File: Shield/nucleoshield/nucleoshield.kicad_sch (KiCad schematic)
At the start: 21 parts, among them J1 Conn_02x19_Odd_Even, J2 Conn_02x19_Odd_Even

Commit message: Nucleo shield
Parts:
- added J? (x2): Screw_Terminal_01x02, Connector_TE-Connectivity:TE_826576-2_1x02_P3.96mm_Vertical, symbol Connector:Screw_Terminal_01x02
- added JP?: Jumper_3_Open, symbol Jumper:Jumper_3_Open
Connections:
- net Nucleo_3V3 is gone; now on net NUCLEO_3V3: JP?.1 (A)
- net DCDC_3V3: now also J?.1 (Pin_1)
- net 3V3 renamed NUCLEO_3V3
- net 5V renamed NUCLEO_5V
- net NUCLEO_5V: now also JP?.1 (A)
- new net DCDC_5V: J?.1 (Pin_1), JP?.3 (B)
- new net DCDC_GND: J?.2 (Pin_2), J?.2 (Pin_2)
- new net LOGIC_5V: JP?.2 (C)
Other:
- moved on the sheet: C?, D?, IC?, R?

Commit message: Schematic and pcb ready
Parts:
- removed C?: 100n, symbol Device:C
- removed C? (x3): 0.1u, symbol Device:C
- removed IC?: L80-M39, L80-M39, symbol L80-M39:L80-M39
- removed J? (x3): Conn_01x05, Connector_PinSocket_2.54mm:PinSocket_1x05_P2.54mm_Vertical, symbol Connector_Generic:Conn_01x05
- removed J? (x2): Screw_Terminal_01x02, Connector_TE-Connectivity:TE_826576-2_1x02_P3.96mm_Vertical, symbol Connector:Screw_Terminal_01x02
- removed JP? (x2): Jumper_3_Open, symbol Jumper:Jumper_3_Open
- removed R? (x2): R, symbol Device:R
- removed U?: ICM-20948, Sensor_Motion:InvenSense_QFN-24_3x3mm_P0.4mm, symbol Sensor_Motion:ICM-20948
- added C1, C5: 470u, Capacitor_THT:CP_Radial_D8.0mm_P3.50mm, symbol Device:C_Polarized
- added C2: 47u, Capacitor_SMD:C_1206_3216Metric, symbol Device:C
- added C3, C4: 100n, Capacitor_SMD:C_1206_3216Metric, symbol Device:C
- added IC1: L80-M39, componentLib:L80-M39, symbol L80-M39:L80-M39
- added J11: MPU9250, Connector_PinHeader_2.54mm:PinHeader_1x10_P2.54mm_Vertical, symbol Connector_Generic:Conn_01x10
- added J3: POWER, Connector_PinHeader_2.54mm:PinHeader_1x03_P2.54mm_Vertical, symbol Connector_Generic:Conn_01x03
- added J4: MOTOR_1, Connector_PinSocket_2.54mm:PinSocket_1x04_P2.54mm_Vertical, symbol Connector_Generic:Conn_01x04
- added J7: MOTOR_2, Connector_PinSocket_2.54mm:PinSocket_1x04_P2.54mm_Vertical, symbol Connector_Generic:Conn_01x04
- added J8: LCD_I2C, Connector_PinSocket_2.54mm:PinSocket_1x04_P2.54mm_Vertical, symbol Connector_Generic:Conn_01x04
- added J9: MOTOR_3, Connector_PinSocket_2.54mm:PinSocket_1x04_P2.54mm_Vertical, symbol Connector_Generic:Conn_01x04
- added JP1: AVDD-3.3V, Jumper:SolderJumper-2_P1.3mm_Bridged2Bar_Pad1.0x1.5mm, symbol Jumper:Jumper_2_Bridged
- added Q1, Q2: BSS138, Package_TO_SOT_SMD:SOT-23, symbol Transistor_FET:BSS138
- added R1: 10k, Resistor_SMD:R_0805_2012Metric, symbol Device:R
- added R2: 2k, Resistor_SMD:R_0805_2012Metric, symbol Device:R
- added R3, R4, R5, R6: 2K, Resistor_SMD:R_0805_2012Metric, symbol Device:R
- added TP1: AVDD, TestPoint:TestPoint_THTPad_1.0x1.0mm_Drill0.5mm, symbol Connector:TestPoint
- C6, C7: renamed from C?; footprint (none) -> Capacitor_SMD:C_1206_3216Metric
- D1: renamed from D?; footprint (none) -> LED_SMD:LED_0805_2012Metric
- J10: renamed from J?; value Conn_01x04 -> ENCODER_3; footprint (none) -> Connector_PinSocket_2.54mm:PinSocket_1x04_P2.54mm_Vertical
- J5: renamed from J?; value Conn_01x04 -> ENCODER_1
- J6: renamed from J?; value Conn_01x04 -> ENCODER_2; footprint (none) -> Connector_PinSocket_2.54mm:PinSocket_1x04_P2.54mm_Vertical
- R7: renamed from R?; value R -> 1K; footprint (none) -> Resistor_SMD:R_0805_2012Metric
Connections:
- net GND is gone; now on net ENCODER_GND: J1.19 (Pin_19), J1.20 (Pin_20), J1.22 (Pin_22), J1.8 (Pin_8), J2.20 (Pin_20), J2.9 (Pin_9)
- net LOGIC_GND is gone; now on net ENCODER_GND: C6.1, C7.1, D1.1 (K)
- net NUCLEO_3V3 is gone; now on net ENCODER_VCC: J1.16 (Pin_16)
- net NUCLEO_5V is gone; now on net LOGIC_5V: J1.18 (Pin_18)
- net AVDD: now also JP1.1 (A), TP1.1
- net E5V: now also J3.2 (5V_DCDC)
- net ENCODER_A1: now also J1.23 (Pin_23), J5.3 (Pin_3); no longer J5.2 (Pin_2)
- net ENCODER_A2: now also J1.27 (Pin_27), J6.3 (Pin_3); no longer J6.2 (Pin_2)
- net ENCODER_A3: now also J1.31 (Pin_31), J10.3 (Pin_3); no longer J10.2 (Pin_2)
- net ENCODER_B1: now also J1.25 (Pin_25), J5.4 (Pin_4); no longer J5.1 (Pin_1)
- net ENCODER_B2: now also J1.29 (Pin_29), J6.4 (Pin_4); no longer J6.1 (Pin_1)
- net ENCODER_B3: now also J1.35 (Pin_35), J10.4 (Pin_4); no longer J10.1 (Pin_1)
- net ENCODER_GND: now also J10.2 (Pin_2), J5.2 (Pin_2), J6.2 (Pin_2), C1.2, C2.1, C3.2, C4.2, C5.2, IC1.12 (GND_2), IC1.3 (GND_1), J11.2 (Pin_2), J3.3 (GND), J4.2 (Pin_2), J7.2 (Pin_2), J8.2 (Pin_2), J9.2 (Pin_2), R2.2; no longer J10.3 (Pin_3), J10.4 (Pin_4), J5.3 (Pin_3), J5.4 (Pin_4), J6.3 (Pin_3), J6.4 (Pin_4)
- net GPS_RESET: now also IC1.10 (RESET)
- net GPS_UART_RX: now also IC1.1 (RXD1)
- net GPS_UART_TX: now also IC1.2 (TXD1)
- net INA1: now also J4.3 (Pin_3)
- net INA2: now also J7.3 (Pin_3)
- net INA3: now also J9.3 (Pin_3)
- net INB1: now also J4.4 (Pin_4)
- net INB2: now also J7.4 (Pin_4)
- net INB3: now also J9.4 (Pin_4)
- net LOGIC_5V: now also C3.1, C5.1, J8.1 (Pin_1), R5.1, R6.1
- net SCL: now also J11.3 (Pin_3)
- net SDA: now also J11.4 (Pin_4)
- net VIN: now also J3.1 (7.2V), R1.1
- net at R7.2: now also IC1.6 (1PPS)
- net BAT_ADC: now reaches J1.38 (Pin_38)
- net BAT_ADC: now also C2.2, R1.2, R2.1
- net SCL2: now reaches J2.25 (Pin_25)
- net SCL2: now also Q2.2 (S), R4.2
- net SDA2: now reaches J2.31 (Pin_31)
- net SDA2: now also Q1.2 (S), R3.2
- net AD0: no longer names the net of J2.15 (Pin_15)
- net AGND: no longer names the net of J2.32 (Pin_32)
- net LOGIC_3V3 renamed ENCODER_VCC
- net ENCODER_VCC: now also J10.1 (Pin_1), J5.1 (Pin_1), J6.1 (Pin_1), C1.1, C4.1, IC1.4 (VCC), IC1.5 (V_BCKP), J11.1 (Pin_1), J4.1 (Pin_1), J7.1 (Pin_1), J9.1 (Pin_1), JP1.2 (B), Q1.1 (G), Q2.1 (G), R3.1, R4.1
- net MODE1: no longer names the net of J2.12 (Pin_12)
- net MODE2: no longer names the net of J2.14 (Pin_14)
- net MODE3: no longer names the net of J2.16 (Pin_16)
- new net: J8.3 (Pin_3), Q1.3 (D), R5.2
- new net: J8.4 (Pin_4), Q2.3 (D), R6.2
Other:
- note added: "5V I2C interface"
- note added: "LCD"
- moved on the sheet: R7

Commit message: power modifications
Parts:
- added JP2: Jumper_3_Open, Connector_PinSocket_2.54mm:PinSocket_1x03_P2.54mm_Vertical, symbol Jumper:Jumper_3_Open
- J10, J4, J5, J6, J7, J8, J9: footprint Connector_PinSocket_2.54mm:PinSocket_1x04_P2.54mm_Vertical -> Connector_JST:JST_EH_B4B-EH-A_1x04_P2.50mm_Vertical
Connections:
- net LOGIC_5V: now also JP2.2 (C); no longer J1.18 (Pin_18)
- net E5V renamed 5V_DCDC
- net 5V_DCDC: now also JP2.3 (B)
- new net NUCLEO_5V: J1.18 (Pin_18), JP2.1 (A)
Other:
- moved on the sheet: C2, C3, C5, J3, JP1, R1, R2, TP1

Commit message: Power connector
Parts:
- added J12, J13: Screw_Terminal_01x02, TerminalBlock:TerminalBlock_Altech_AK300-2_P5.00mm, symbol Connector:Screw_Terminal_01x02
- added JP3: Jumper_3_Open, Connector_PinSocket_2.54mm:PinSocket_1x03_P2.54mm_Vertical, symbol Jumper:Jumper_3_Open
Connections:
- net 5V_DCDC: now also J12.2 (Pin_2)
- net ENCODER_GND: now also J12.1 (Pin_1), J13.1 (Pin_1)
- net ENCODER_VCC: now also JP3.2 (C); no longer J1.16 (Pin_16), JP1.2 (B)
- new net 3V3_DCDC: J13.2 (Pin_2), JP3.3 (B)
- new net NUCLEO_3V3: J1.16 (Pin_16), JP1.2 (B), JP3.1 (A)
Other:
- moved on the sheet: C1, C2, C3, C4, C5, J3, JP1, JP2, R1, R2, TP1

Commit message: small changes
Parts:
- JP2, JP3: footprint Connector_PinSocket_2.54mm:PinSocket_1x03_P2.54mm_Vertical -> Connector_PinHeader_2.54mm:PinHeader_1x03_P2.54mm_Vertical
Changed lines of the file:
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@@
     (property "Reference" "JP2" (id 0) (at 38.1 67.945 0))
     (property "Value" "Jumper_3_Open" (id 1) (at 38.1 70.485 0))
-    (property "Footprint" "Connector_PinSocket_2.54mm:PinSocket_1x03_P2.54mm_Vertical" (id 2) (at 38.1 74.93 0)
+    (property "Footprint" "Connector_PinHeader_2.54mm:PinHeader_1x03_P2.54mm_Vertical" (id 2) (at 38.1 74.93 0)
       (effects (font (size 1.27 1.27)) hide)
     )
@@
     (property "Reference" "JP3" (id 0) (at 33.02 23.495 0))
     (property "Value" "Jumper_3_Open" (id 1) (at 33.02 26.035 0))
-    (property "Footprint" "Connector_PinSocket_2.54mm:PinSocket_1x03_P2.54mm_Vertical" (id 2) (at 33.02 30.48 0)
+    (property "Footprint" "Connector_PinHeader_2.54mm:PinHeader_1x03_P2.54mm_Vertical" (id 2) (at 33.02 30.48 0)
       (effects (font (size 1.27 1.27)) hide)
     )
@@
     )
     (path "/1d784b1d-1a08-453a-ad94-19f28f2d2290"
-      (reference "JP2") (unit 1) (value "Jumper_3_Open") (footprint "Connector_PinSocket_2.54mm:PinSocket_1x03_P2.54mm_Vertical")
+      (reference "JP2") (unit 1) (value "Jumper_3_Open") (footprint "Connector_PinHeader_2.54mm:PinHeader_1x03_P2.54mm_Vertical")
     )
     (path "/6e750300-c15d-40a5-8bda-8418a557aac4"
-      (reference "JP3") (unit 1) (value "Jumper_3_Open") (footprint "Connector_PinSocket_2.54mm:PinSocket_1x03_P2.54mm_Vertical")
+      (reference "JP3") (unit 1) (value "Jumper_3_Open") (footprint "Connector_PinHeader_2.54mm:PinHeader_1x03_P2.54mm_Vertical")
     )
     (path "/3c113301-69e8-4565-8218-7206db335ff7"

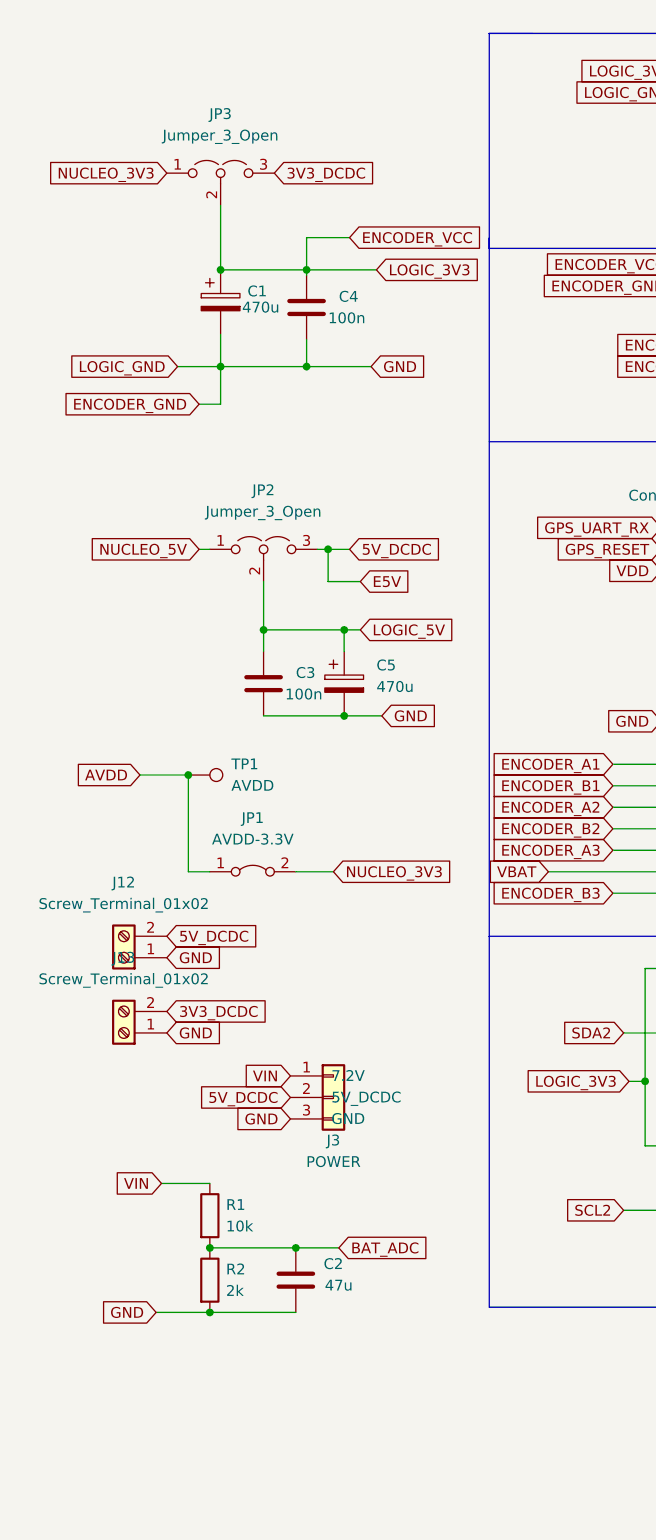
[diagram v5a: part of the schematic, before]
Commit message: Csatlakozók megváltoztatva, polaritásvédelem, apróbb javítások
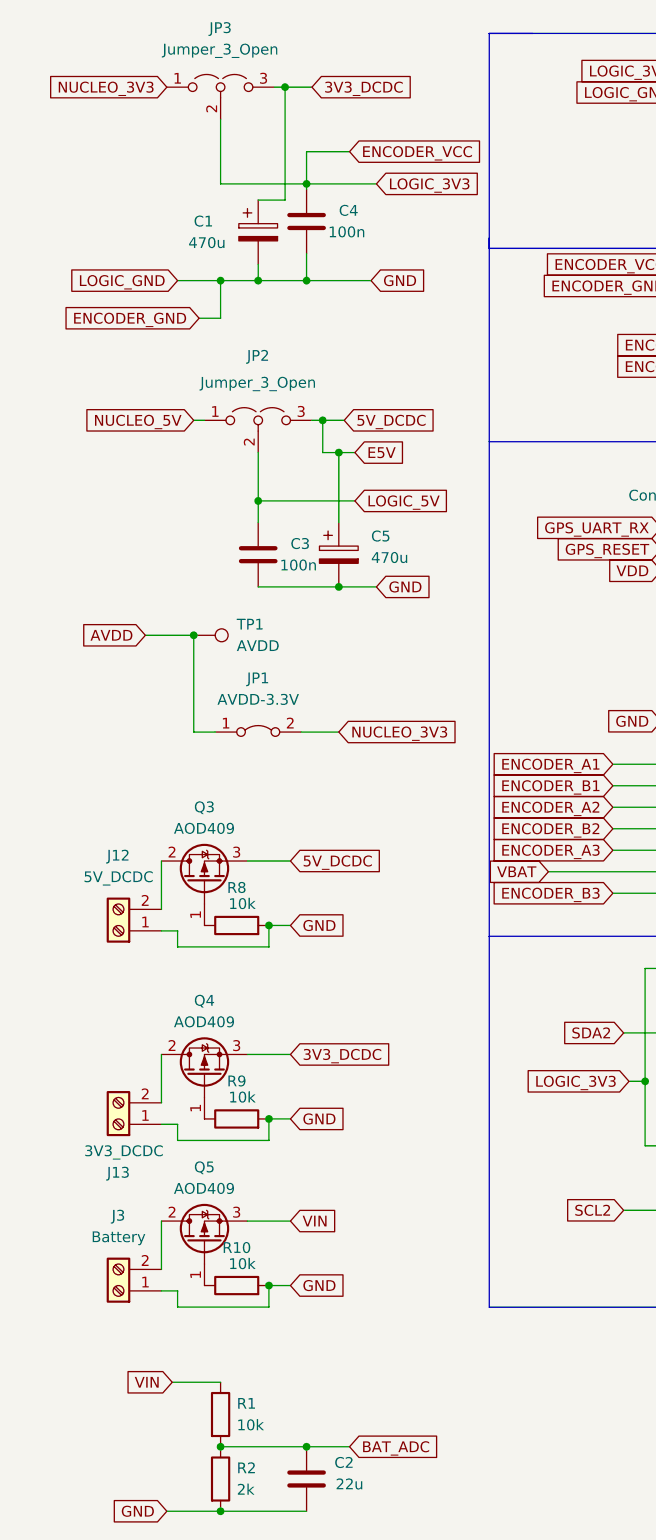
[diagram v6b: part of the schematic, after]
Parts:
- removed J3: POWER, Connector_PinHeader_2.54mm:PinHeader_1x03_P2.54mm_Vertical, symbol Connector_Generic:Conn_01x03
- added J3: Battery, TerminalBlock:TerminalBlock_Altech_AK300-2_P5.00mm, symbol Connector:Screw_Terminal_01x02
- added Q3, Q4, Q5: AOD409, Package_TO_SOT_SMD:TO-252-2, symbol Transistor_FET:AO3401A
- added R10, R8, R9: 10k, Resistor_SMD:R_0805_2012Metric, symbol Device:R
- C2: value 47u -> 22u
- J12: value Screw_Terminal_01x02 -> 5V_DCDC
- J13: value Screw_Terminal_01x02 -> 3V3_DCDC
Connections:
- net 3V3_DCDC: now also C1.1, Q4.3 (S); no longer J13.2 (Pin_2)
- net 5V_DCDC: now also C5.1, Q3.3 (S); no longer J12.2 (Pin_2)
- net ENCODER_GND: now also J3.1 (Pin_1), R10.2, R8.2, R9.2
- net ENCODER_VCC: no longer C1.1
- net LOGIC_5V: no longer C5.1
- net VIN: now also Q5.3 (S)
- new net: Q3.1 (G), R8.1
- new net: Q5.1 (G), R10.1
- new net: J3.2 (Pin_2), Q5.2 (D)
- new net: Q4.1 (G), R9.1
- new net: J13.2 (Pin_2), Q4.2 (D)
- new net: J12.2 (Pin_2), Q3.2 (D)
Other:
- moved on the sheet: C1, C2, C3, C4, C5, J12, J13, JP1, JP2, JP3, R1, R2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

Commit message: Fetek kicserélve
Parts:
- Q3, Q4, Q5: value AOD409 -> AO3401A; footprint Package_TO_SOT_SMD:TO-252-2 -> Package_TO_SOT_SMD:SOT-23
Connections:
- net 3V3_DCDC: now also Q4.2 (S); no longer Q4.3 (S)
- net 5V_DCDC: now also Q3.2 (S); no longer Q3.3 (S)
- net VIN: now also Q5.2 (S); no longer Q5.3 (S)
- net at J3.2 (Pin_2): now also Q5.3 (D); no longer Q5.2 (D)
- net at J13.2 (Pin_2): now also Q4.3 (D); no longer Q4.2 (D)
- net at J12.2 (Pin_2): now also Q3.3 (D); no longer Q3.2 (D)
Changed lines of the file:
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@@
     (pin "2")
-  )
-  (symbol (lib_id "Transistor_FET:AO3401A") (at 31.115 156.845 90) (unit 1)
-    (in_bom yes) (on_board yes)
-    (property "Reference" "Q5" (id 0) (at 31.115 147.955 90))
-    (property "Value" "AOD409" (id 1) (at 31.115 150.495 90))
-    (property "Footprint" "Package_TO_SOT_SMD:TO-252-2" (id 2) (at 24.765 151.765 0)
-      (effects (font (size 1.27 1.27) italic) (justify left) hide)
-    )
-    (property "Datasheet" "http://www.aosmd.com/pdfs/datasheet/AO3401A.pdf" (id 3) (at 31.115 156.845 0)
-      (effects (font (size 1.27 1.27)) (justify left) hide)
-    )
-    (pin "1")
-    (pin "2")
-    (pin "3")
   )
   (symbol (lib_id "Jumper:Jumper_3_Open") (at 37.465 59.69 0) (unit 1)
@@
     (pin "1")
     (pin "2")
-  )
-  (symbol (lib_id "Transistor_FET:AO3401A") (at 31.115 137.16 90) (unit 1)
-    (in_bom yes) (on_board yes)
-    (property "Reference" "Q4" (id 0) (at 31.115 128.27 90))
-    (property "Value" "AOD409" (id 1) (at 31.115 130.81 90))
-    (property "Footprint" "Package_TO_SOT_SMD:TO-252-2" (id 2) (at 24.765 132.08 0)
-      (effects (font (size 1.27 1.27) italic) (justify left) hide)
-    )
-    (property "Datasheet" "http://www.aosmd.com/pdfs/datasheet/AO3401A.pdf" (id 3) (at 31.115 137.16 0)
-      (effects (font (size 1.27 1.27)) (justify left) hide)
-    )
-    (pin "1")
-    (pin "2")
-    (pin "3")
   )
   (symbol (lib_id "Device:C") (at 251.46 38.1 0) (unit 1)
@@
     (pin "1")
     (pin "2")
-  )
-  (symbol (lib_id "Transistor_FET:AO3401A") (at 31.115 114.3 90) (unit 1)
-    (in_bom yes) (on_board yes)
-    (property "Reference" "Q3" (id 0) (at 31.115 105.41 90))
-    (property "Value" "AOD409" (id 1) (at 31.115 107.95 90))
-    (property "Footprint" "Package_TO_SOT_SMD:TO-252-2" (id 2) (at 24.765 109.22 0)
-      (effects (font (size 1.27 1.27) italic) (justify left) hide)
-    )
-    (property "Datasheet" "http://www.aosmd.com/pdfs/datasheet/AO3401A.pdf" (id 3) (at 31.115 114.3 0)
-      (effects (font (size 1.27 1.27)) (justify left) hide)
-    )
-    (pin "1")
-    (pin "2")
-    (pin "3")
   )
   (symbol (lib_id "Connector_Generic:Conn_01x04") (at 137.16 138.43 0) (unit 1)
@@
     (pin "1")
   )
+  (symbol (lib_name "AO3401A_1") (lib_id "Transistor_FET:AO3401A") (at 31.115 156.845 90) (unit 1)
+    (in_bom yes) (on_board yes) (fields_autoplaced)
+    (property "Reference" "Q5" (id 0) (at 31.115 147.32 90))
+    (property "Value" "AO3401A" (id 1) (at 31.115 149.86 90))
+    (property "Footprint" "Package_TO_SOT_SMD:SOT-23" (id 2) (at 33.02 151.765 0)
+      (effects (font (size 1.27 1.27) italic) (justify left) hide)
+    )
+    (property "Datasheet" "http://www.aosmd.com/pdfs/datasheet/AO3401A.pdf" (id 3) (at 31.115 156.845 0)
+      (effects (font (size 1.27 1.27)) (justify left) hide)
+    )
+    (pin "1")
+    (pin "2")
+    (pin "3")
+  )
   (symbol (lib_id "L80-M39:L80-M39") (at 199.39 36.83 0) (unit 1)
     (in_bom yes) (on_board yes) (fields_autoplaced)
@@
     (pin "4")
   )
+  (symbol (lib_name "AO3401A_1") (lib_id "Transistor_FET:AO3401A") (at 31.115 137.16 90) (unit 1)
+    (in_bom yes) (on_board yes) (fields_autoplaced)
+    (property "Reference" "Q4" (id 0) (at 31.115 127.635 90))
+    (property "Value" "AO3401A" (id 1) (at 31.115 130.175 90))
+    (property "Footprint" "Package_TO_SOT_SMD:SOT-23" (id 2) (at 33.02 132.08 0)
+      (effects (font (size 1.27 1.27) italic) (justify left) hide)
+    )
+    (property "Datasheet" "http://www.aosmd.com/pdfs/datasheet/AO3401A.pdf" (id 3) (at 31.115 137.16 0)
+      (effects (font (size 1.27 1.27)) (justify left) hide)
+    )
+    (pin "1")
+    (pin "2")
+    (pin "3")
+  )
   (symbol (lib_id "Device:R") (at 33.02 184.785 0) (unit 1)
     (in_bom yes) (on_board yes) (fields_autoplaced)
@@
     (pin "1")
     (pin "2")
+  )
+  (symbol (lib_name "AO3401A_1") (lib_id "Transistor_FET:AO3401A") (at 31.115 114.3 90) (unit 1)
+    (in_bom yes) (on_board yes) (fields_autoplaced)
+    (property "Reference" "Q3" (id 0) (at 31.115 104.775 90))
+    (property "Value" "AO3401A" (id 1) (at 31.115 107.315 90))
+    (property "Footprint" "Package_TO_SOT_SMD:SOT-23" (id 2) (at 33.02 109.22 0)
+      (effects (font (size 1.27 1.27) italic) (justify left) hide)
+    )
+    (property "Datasheet" "http://www.aosmd.com/pdfs/datasheet/AO3401A.pdf" (id 3) (at 31.115 114.3 0)
+      (effects (font (size 1.27 1.27)) (justify left) hide)
+    )
+    (pin "1")
+    (pin "2")
+    (pin "3")
   )
   (symbol (lib_id "Device:R") (at 34.925 161.925 90) (unit 1)
@@
       (reference "Q2") (unit 1) (value "BSS138") (footprint "Package_TO_SOT_SMD:SOT-23")
     )
-    (path "/98008f3c-4986-4f71-a93e-48a627121a13"
-      (reference "Q3") (unit 1) (value "AOD409") (footprint "Package_TO_SOT_SMD:TO-252-2")
-    )
-    (path "/2e0f0119-a2ac-4f17-829f-6557a399ef8d"
-      (reference "Q4") (unit 1) (value "AOD409") (footprint "Package_TO_SOT_SMD:TO-252-2")
-    )
-    (path "/1a9a2bed-aa21-495a-bc5a-d15840c38fe3"
-      (reference "Q5") (unit 1) (value "AOD409") (footprint "Package_TO_SOT_SMD:TO-252-2")
+    (path "/ee5a6182-1c97-4a49-b12b-c89c78a6cca4"
+      (reference "Q3") (unit 1) (value "AO3401A") (footprint "Package_TO_SOT_SMD:SOT-23")
+    )
+    (path "/e8fd9f75-e1a2-4ac1-b7e3-8d8b9fb1f177"
+      (reference "Q4") (unit 1) (value "AO3401A") (footprint "Package_TO_SOT_SMD:SOT-23")
+    )
+    (path "/cea75623-64e5-4977-9f31-6128e61a1b0e"
+      (reference "Q5") (unit 1) (value "AO3401A") (footprint "Package_TO_SOT_SMD:SOT-23")
     )
     (path "/40fa17f7-2a1d-4731-bfb7-aed09dc0723c"
